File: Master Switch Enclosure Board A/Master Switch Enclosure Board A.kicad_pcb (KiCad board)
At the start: 2 copper layers, 100 x 50 mm, 3 parts, among them IC1 LM5155DSSR, Q1 CSD18537NQ5A

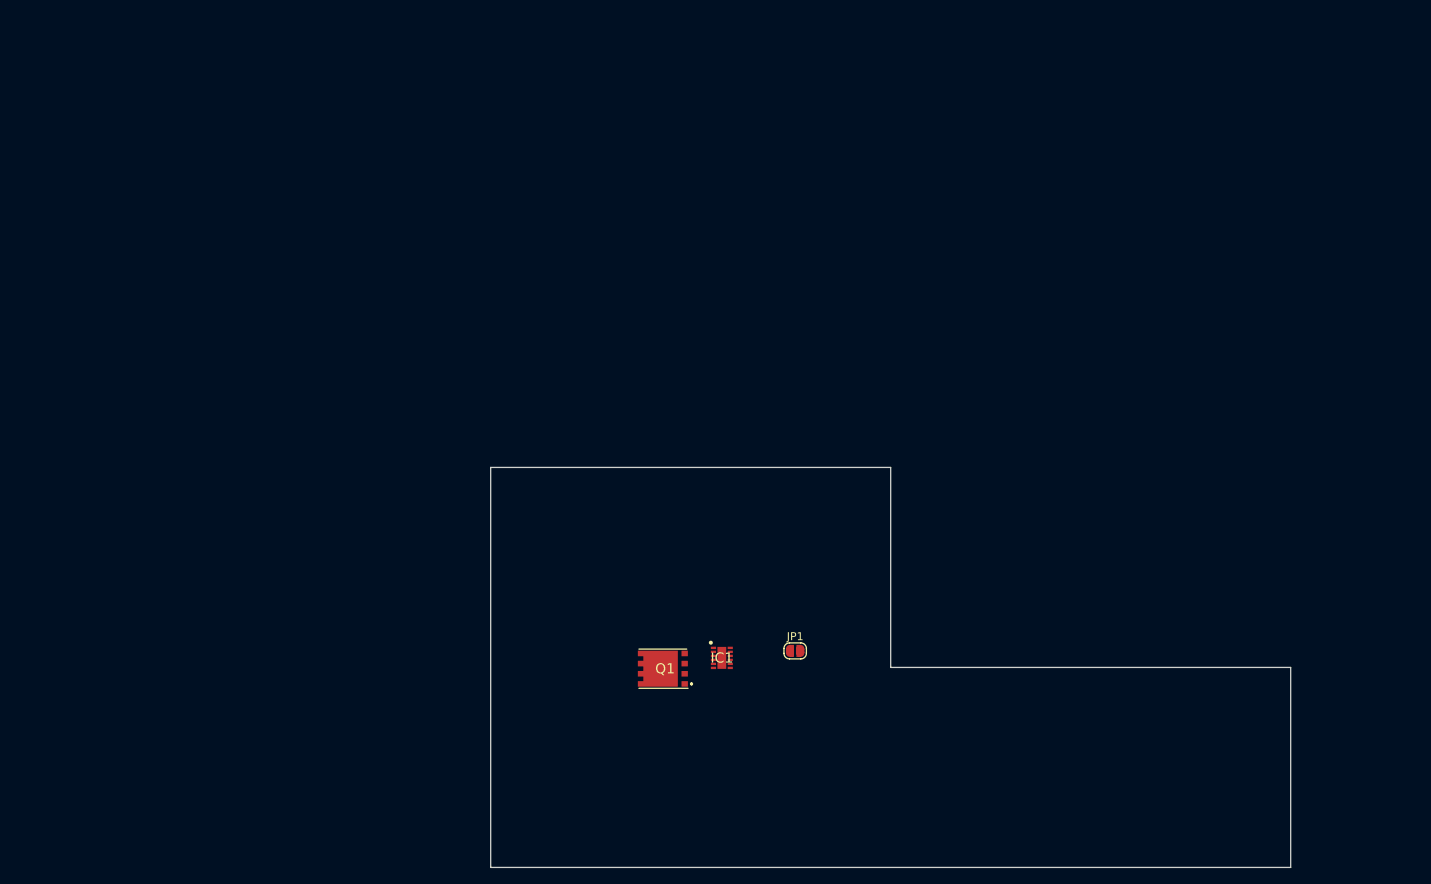
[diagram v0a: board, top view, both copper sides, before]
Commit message: PCB partial layout
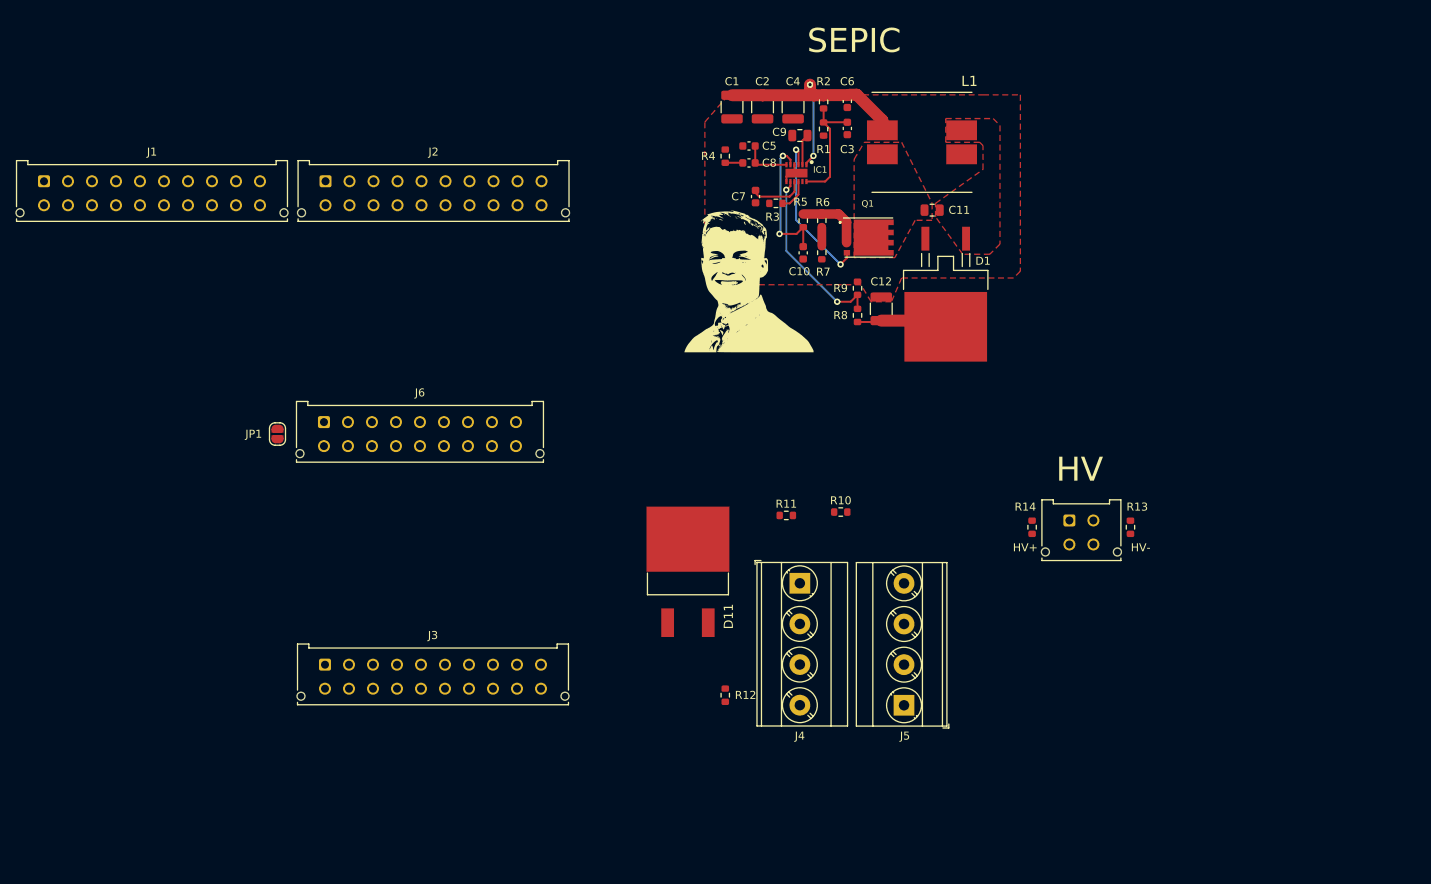
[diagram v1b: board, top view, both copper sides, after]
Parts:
- added C1: 10u, Capacitor_SMD:C_1210_3225Metric, F.Cu at (130.2, 55.0)
- added C10: 100p, Capacitor_SMD:C_0603_1608Metric, F.Cu at (139.1, 73.2)
- added C11: 9.4u, Capacitor_SMD:C_0805_2012Metric, F.Cu at (155.2, 67.8)
- added C12: 66u, Capacitor_SMD:C_1210_3225Metric, F.Cu at (148.8, 80.2)
- added C2: 10u, Capacitor_SMD:C_1210_3225Metric, F.Cu at (134.0, 55.0)
- added C3: 100p, Capacitor_SMD:C_0603_1608Metric, F.Cu at (144.6, 57.6)
- added C4: 10u, Capacitor_SMD:C_1210_3225Metric, F.Cu at (137.8, 55.0)
- added C5: 270p, Capacitor_SMD:C_0603_1608Metric, F.Cu at (132.3, 59.8)
- added C6: 100n, Capacitor_SMD:C_0603_1608Metric, F.Cu at (144.6, 54.2)
- added C7: 220n, Capacitor_SMD:C_0603_1608Metric, F.Cu at (133.1, 66.1)
- added C8: 6.8n, Capacitor_SMD:C_0603_1608Metric, F.Cu at (132.3, 61.9)
- added C9: 1u, Capacitor_SMD:C_0805_2012Metric, F.Cu at (138.6, 58.5)
- added D1: STPS20M100SG-TR, Global Libraries:STPS20M100SG-TR, F.Cu at (156.9, 80.2)
- added D11: D_Schottky, Global Libraries:MBRB41H100CTT4G, F.Cu at (124.7, 114.2)
- added G***: LOGO, Global Libraries:rylan, F.Cu at (130.4, 75.6)
- added J1: Harness In A, Connector_Molex:Molex_Micro-Fit_3.0_43045-2012_2x10_P3.00mm_Vertical, F.Cu at (44.2, 64.2)
- added J2: Harness In B, Connector_Molex:Molex_Micro-Fit_3.0_43045-2012_2x10_P3.00mm_Vertical, F.Cu at (79.4, 64.2)
- added J3: Harness Out, Connector_Molex:Molex_Micro-Fit_3.0_43045-2012_2x10_P3.00mm_Vertical, F.Cu at (79.3, 124.7)
- added J4: Screw_Terminal_01x04, TerminalBlock_Phoenix:TerminalBlock_Phoenix_MKDS-3-4-5.08_1x04_P5.08mm_Horizontal, F.Cu at (138.6, 114.5)
- added J5: Screw_Terminal_01x04, TerminalBlock_Phoenix:TerminalBlock_Phoenix_MKDS-3-4-5.08_1x04_P5.08mm_Horizontal, F.Cu at (151.7, 129.7)
- added J6: 18-pin MicroFit, Connector_Molex:Molex_Micro-Fit_3.0_43045-1812_2x09_P3.00mm_Vertical, F.Cu at (79.2, 94.3)
- added J7: 4-pin MicroFit, Connector_Molex:Molex_Micro-Fit_3.0_43045-0412_2x02_P3.00mm_Vertical, F.Cu at (172.3, 106.6)
- added L1: 7448700015, Global Libraries:WE-DD_12XX_CROSSED12, F.Cu at (153.9, 59.4)
- added R1: 6k8, Resistor_SMD:R_0603_1608Metric, F.Cu at (141.6, 57.7)
- added R10: 100k, Resistor_SMD:R_0603_1608Metric, F.Cu at (143.8, 105.6)
- added R11: 15k, Resistor_SMD:R_0603_1608Metric, F.Cu at (137.0, 106.0)
- added R12: 100k, Resistor_SMD:R_0603_1608Metric, F.Cu at (129.3, 128.5)
- added R13: 15k, Resistor_SMD:R_0603_1608Metric, F.Cu at (180.0, 107.5)
- added R14: 15k, Resistor_SMD:R_0603_1608Metric, F.Cu at (167.7, 107.5)
- added R2: 34k8, Resistor_SMD:R_0603_1608Metric, F.Cu at (141.6, 54.3)
- added R3: 17k8, Resistor_SMD:R_0603_1608Metric, F.Cu at (135.7, 67.0)
- added R4: 10k, Resistor_SMD:R_0603_1608Metric, F.Cu at (129.3, 61.1)
- added R5: 100, Resistor_SMD:R_0603_1608Metric, F.Cu at (139.1, 69.1)
- added R6: 4m, Resistor_SMD:R_0603_1608Metric, F.Cu at (141.4, 69.1)
- added R7: 4m, Resistor_SMD:R_0603_1608Metric, F.Cu at (141.4, 73.2)
- added R8: 51k1, Resistor_SMD:R_0603_1608Metric, F.Cu at (145.9, 81.0)
- added R9: 4k7, Resistor_SMD:R_0603_1608Metric, F.Cu at (145.9, 77.6)
- moved JP1 70.2 mm to (73.4, 95.8), turned to 90 degrees
- moved IC1 61.3 mm to (138.2, 63.2), turned to -90 degrees
- moved Q1 59.5 mm to (147.0, 71.3), turned to 180 degrees
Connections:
- IC1 pad 1: LV_out -> LV_mastersw_out
- JP1 pad 2: Net-(J8-Pad1) -> EM_12V
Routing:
- net LV_mastersw_out: track 0.00 -> 33.1 mm, vias 0 -> 2
- net /SEPIC/FB: track 0.00 -> 22.6 mm, vias 0 -> 2
- net Net-(IC1-Pad3): track 0.00 -> 20.5 mm, vias 0 -> 2
- net Net-(C10-Pad2): track 0.00 -> 17.4 mm, vias 0 -> 2
- net /SEPIC/UVLO: track 0.00 -> 15.0 mm
- net SEPIC_out: track 0.00 -> 11.4 mm
- net Net-(Q1-Pad1): track 0.00 -> 8.42 mm
- net /SEPIC/SS: track 0.00 -> 6.91 mm
- net /SEPIC/COMP: track 0.00 -> 6.12 mm
- net /SEPIC/RT: track 0.00 -> 4.08 mm
- net Net-(C9-Pad2): track 0.00 -> 3.91 mm
- net GND: track 0.00 -> 3.20 mm
- net Net-(R6-Pad2): track 0.00 -> 2.36 mm
- net Net-(C8-Pad2): track 0.00 -> 2.20 mm
- added copper zone on F.Cu, net GND
- added copper zone on F.Cu, net Net-(C11-Pad1)
- added copper zone on F.Cu, net Net-(C11-Pad2)
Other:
- board outline removed
- board text added: "HV"
- board text added: "HV+"
- board text added: "HV-"
- board text added: "SEPIC"

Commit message: tsmp tanky resistor
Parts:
- R13, R14: footprint Resistor_SMD:R_0603_1608Metric -> Global Libraries:355015KFT
- moved C10 59.4 mm to (188.3, 106.3)
- moved C1 59.4 mm to (179.4, 88.0)
- moved C11 59.4 mm to (204.5, 100.9)
- moved C3 59.4 mm to (193.9, 90.7)
- moved C6 59.4 mm to (193.9, 87.3)
- moved C7 59.4 mm to (182.4, 99.2)
- moved C9 59.4 mm to (187.9, 91.6)
- moved D1 59.4 mm to (206.2, 113.3)
- moved G*** 59.4 mm to (179.6, 108.7)
- moved Q1 59.4 mm to (196.3, 104.4)
- moved R5 59.4 mm to (188.4, 102.2)
- moved C5 59.4 mm to (181.6, 92.9)
- moved R9 59.4 mm to (195.1, 110.7)
- moved C12 59.4 mm to (198.1, 113.3)
- moved C2 59.4 mm to (183.3, 88.0)
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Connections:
- J2 pad 17: unconnected-(J2-Pad17) -> GND
- J3 pad 20: unconnected-(J3-Pad20) -> GND
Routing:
- net HV-: track 0.00 -> 10.0 mm
- net HV+: track 0.00 -> 10.0 mm
- net Net-(J7-Pad4): track 0.00 -> 9.33 mm
- net Net-(J7-Pad3): track 0.00 -> 9.23 mm
